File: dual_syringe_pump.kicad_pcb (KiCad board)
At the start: 2 copper layers, 100 x 84.6 mm, 163 parts, among them J1 USB_C_Receptacle_USB2.0_16P, J2 Barrel_Jack_Switch_Pin3Ring, Q1 SS8050, Q2 SS8050, Q3 SS8050, Q4 SS8050, SW1 boot, SW2 reset, U1 AMS1117-3.3, U2 ESP32-WROOM-32, U3 CH340C, U4 TP5100, U5 XL4015, U6 TMC2209-LA, U7 TMC2209-LA

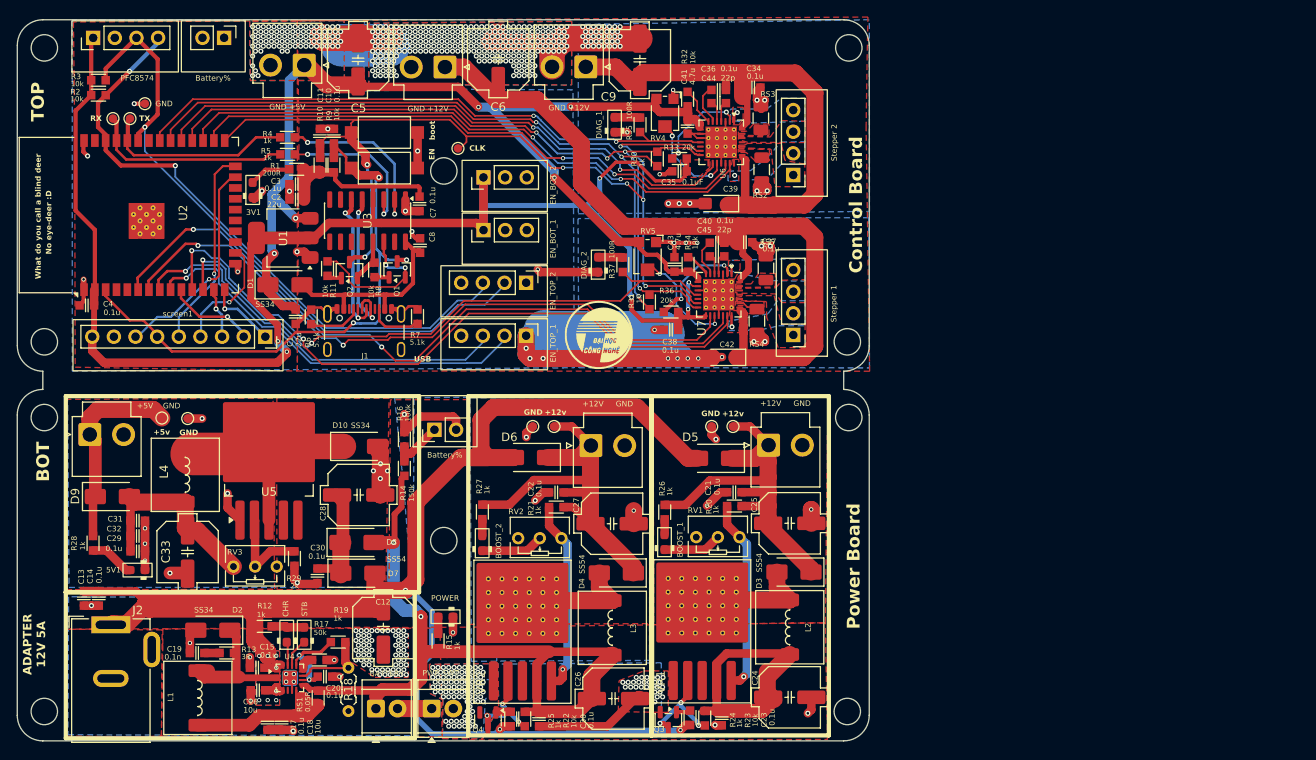
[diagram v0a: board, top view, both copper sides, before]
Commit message: changed to mouse bites
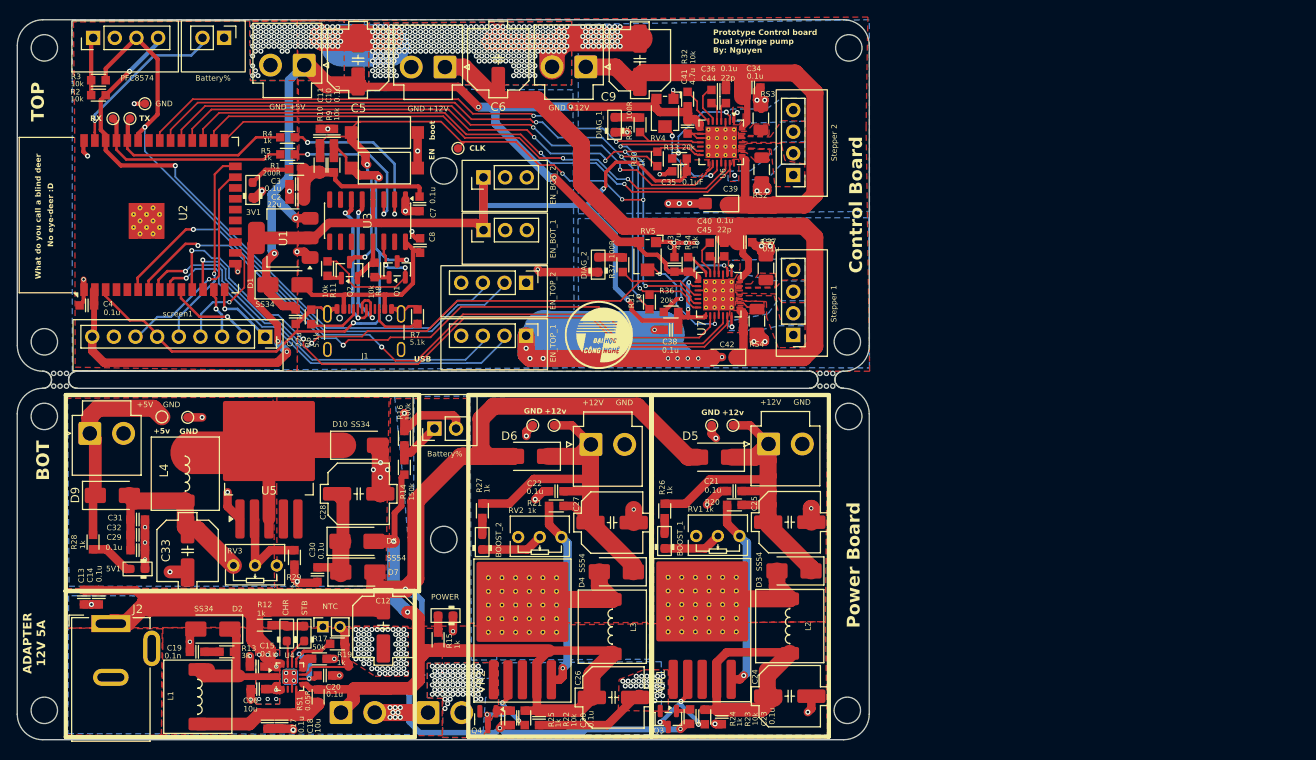
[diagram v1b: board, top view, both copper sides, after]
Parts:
- added mouse-bite-2mm-slot: VAL**, Panelization.pretty-master:mouse-bite-2mm-slot, F.Cu at (109.0, 20.7)
- added mouse-bite-2mm-slot: VAL**, Panelization.pretty-master:mouse-bite-2mm-slot, F.Cu at (19.0, 20.7)
- BATTERY: footprint TerminalBlock_TE-Connectivity:TerminalBlock_TE_282834-2_1x02_P2.54mm_Horizontal -> Connector_JST:JST_VH_B2P-VH-B_1x02_P3.96mm_Vertical; moved to B.Cu
- NTC: renamed from R18; footprint PCM_Resistor_THT_AKL_Double:R_Axial_DIN0204_L3.6mm_D1.6mm_P5.08mm_Horizontal -> Connector_PinSocket_2.00mm:PinSocket_1x02_P2.00mm_Vertical
- PWR SWT: footprint TerminalBlock_TE-Connectivity:TerminalBlock_TE_282834-2_1x02_P2.54mm_Horizontal -> Connector_JST:JST_VH_B2P-VH-B_1x02_P3.96mm_Vertical; moved to B.Cu
- moved NTC 10.3 mm to (49.9, 49.7)
- moved BATTERY 4.12 mm to (52.0, 59.7)
- moved PWR SWT 0.64 mm to (62.2, 59.7)
- moved R19 0.23 mm to (51.6, 51.7)
- moved C12 0.14 mm to (57.0, 49.7)
- moved C18 0.14 mm to (45.0, 60.8)
- moved C20 0.14 mm to (50.1, 55.4)
- moved C21 0.14 mm to (98.2, 33.7)
- moved C30 0.14 mm to (49.2, 43.5)
- moved C30 0.14 mm to (75.2, 60.4)
- moved C33 0.14 mm to (34.0, 40.8)
- moved D2 0.14 mm to (37.0, 49.9)
- moved D3 0.14 mm to (105.2, 43.1)
- moved J2 0.14 mm to (25.0, 49.3)
- moved L1 0.14 mm to (35.2, 57.9)
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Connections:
- Battery% pad 1: unconnected-(bat_%1-Pin_1-Pad1) -> GND1
- Battery% pad 2: unconnected-(bat_%1-Pin_2-Pad2) -> /bat%
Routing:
- net +3.3V: track 204.3 -> 179.8 mm
- net /bat%: track 0.00 -> 19.8 mm, vias 0 -> 1
- net Earth: track 22.5 -> 24.6 mm, vias 75 -> 83
- net /Power Circuits/NTC: track 9.59 -> 11.5 mm
- net Vbat: track 123.3 -> 124.7 mm
- net esp32_CLK: track 117.5 -> 116.2 mm
- net Adapter_+12V: track 186.6 -> 187.2 mm
- net GND: vias 137 -> 124
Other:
- board size 100 x 84.6 mm -> 100 x 84.5 mm
- board text added: "Prototype Control board Dual syringe pump By: Nguyen"
- board text added: "Prototype Power board Dual syringe pump By: Nguyen"

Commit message: post production fixes
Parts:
- removed the NTC at (49.9, 49.7)
- added C46: 1uF, PCM_4ms_Capacitor:C_0603, F.Cu at (46.1, 40.7)
- added NTC: 47d 3950 (10K), Connector_PinHeader_2.00mm:PinHeader_1x02_P2.00mm_Vertical, B.Cu at (52.3, 49.6)
- C1, C2: value 22u -> 22uF
- C10, C13, C15, C17, C20, C21, C22, C23, C3, C30, C31, C34, C36, C37, C38, C4, C40, C7: value 0.1u -> 0.1uF
- C16, C18: value 10u -> 10uF
- C19: value 0.1n -> 0.1nF
- C25, C27: footprint PCM_Capacitor_SMD_Handsoldering_AKL:C_Elec_6.3x7.7 -> PCM_Capacitor_SMD_Handsoldering_AKL:C_Elec_8x10.2
- C41, C43: value 4.7u -> 4.7uF
- C44, C45: value 22p -> 22pF
- D3, D4: footprint Diode_SMD:D_SMA -> Diode_SMD:D_SMC
- L1: footprint PCM_Inductor_SMD_Handsoldering_AKL:L_7.3x7.3_H4.5 -> PCM_Inductor_SMD_Handsoldering_AKL:L_7.3x7.3_H3.5
- L2, L3, L4: footprint PCM_Inductor_SMD_Handsoldering_AKL:L_7.3x7.3_H4.5 -> Inductor_SMD:L_SXN_SMDRI124
- RS1: footprint PCM_4ms_Resistor:R_0603 -> PCM_4ms_Resistor:R_1206_3216Metric
- RV1, RV2, RV3: footprint PCM_Potentiometer_THT_AKL_Double:Potentiometer_Bourns_3266Y_Vertical -> Potentiometer_SMD:Potentiometer_Bourns_TC33X_Vertical
- Steper_1: renamed from Stepper 2
- Steper_2: renamed from Stepper 1
- U4: footprint Package_DFN_QFN:LQFN-16-1EP_3x3mm_P0.5mm_EP1.7x1.7mm -> Package_DFN_QFN:QFN-16-1EP_4x4mm_P0.65mm_EP2.15x2.15mm_ThermalVias
- boost1, boost2: renamed from GND +12V
- boost3, boost4: renamed from +12V     GND
- buck1: renamed from GND +5V
- buck2: renamed from +5V    GND
- power_button1: renamed from PWR SWT
- moved BOOST_2 18.9 mm to (86.2, 32.8), turned to 180 degrees
- moved BOOST_1 18.6 mm to (107.2, 32.8), turned to 180 degrees
- moved C33 16.2 mm to (17.8, 40.7), turned to 90 degrees
- moved R27 14.3 mm to (82.5, 32.8), turned to 180 degrees
- moved 5V1 14.2 mm to (21.6, 30.2), turned to 90 degrees
- moved R26 14.1 mm to (103.7, 32.8), turned to 180 degrees
- moved C27 11.5 mm to (73.2, 33.1), turned to 180 degrees
- moved C25 10.9 mm to (94.7, 33.0), turned to 180 degrees
- moved R28 9.56 mm to (23.3, 30.2), turned to -90 degrees
- moved R21 8.55 mm to (70.0, 39.9), turned to -90 degrees
- moved L4 7.60 mm to (31.4, 39.0)
- moved C21 7.42 mm to (94.2, 27.5)
- moved C22 7.42 mm to (73.0, 27.7)
- moved D9 7.41 mm to (23.2, 41.4), turned to -90 degrees
- moved R20 7.31 mm to (92.2, 39.6), turned to -90 degrees
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- renumbered BATTERY to BAT1, CHR to Chrg1, STB to Stdby1, POWER to bat2, Battery% to bat_%1, Battery% to bat_%2, PFC8574 to buttons_1
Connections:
- R14 pad 2: Net-(bat_%2-Pin_1) -> V_bat%
- R16 pad 1: Net-(bat_%2-Pin_1) -> V_bat%
- R20 pad 1: Net-(VR1-FB) -> GND
- R20 pad 2: +12V_1 -> Net-(VR1-FB)
- R21 pad 1: Net-(VR2-FB) -> GND
- R21 pad 2: +12V_2 -> Net-(VR2-FB)
- RV1 pad 2: GND -> Net-(VR1-FB)
- RV1 pad 3: Net-(VR1-FB) -> +12V_1
- RV2 pad 2: GND -> Net-(VR2-FB)
- RV2 pad 3: Net-(VR2-FB) -> +12V_2
- RV3 pad 1: Net-(D9-A) -> +5V
- U2 pad 37: /bat% -> V_bat%
- U5 pad 4: Net-(D7-K) -> Net-(U5-VC)
- bat_%1 pad 2: /bat% -> V_bat%
- bat_%2 pad 1: Net-(bat_%2-Pin_1) -> V_bat%
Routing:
- net Vbat: track 124.7 -> 43.0 mm
- net Adapter_+12V: track 187.2 -> 121.8 mm, vias 11 -> 13
- net +12V_1: track 114.7 -> 68.3 mm
- net +12V_2: track 141.3 -> 97.7 mm
- net V_bat%: track 0.00 -> 26.3 mm, vias 0 -> 1
- net Net-(D4-A): track 27.5 -> 1.87 mm
- net GND: track 79.6 -> 55.3 mm, vias 124 -> 104
- net +5V: track 149.9 -> 126.3 mm
- net Net-(U4-VS): track 22.6 -> 0.00 mm
- net /bat%: track 19.8 -> 0.00 mm, vias 1 -> 0
- net Net-(D3-A): track 17.2 -> 1.31 mm
- net Net-(D2-K): track 18.6 -> 3.95 mm
- net Earth: track 24.6 -> 17.1 mm, vias 83 -> 35
- net Net-(D9-A): track 23.9 -> 30.9 mm
- net Net-(bat_%2-Pin_1): track 6.42 -> 0.00 mm
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- added copper zone on F.Cu, net Net-(D2-K)
- added copper zone on F.Cu, net Net-(D3-A)
- added copper zone on F.Cu, net Net-(D4-A)
- added copper zone on F.Cu, net Net-(U4-VS)
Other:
- board text added: "12v"
- board text removed: "+12v"
